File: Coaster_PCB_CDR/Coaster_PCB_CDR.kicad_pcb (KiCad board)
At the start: 2 copper layers, 96.6 x 97 mm, 31 parts, among them J1 Vin, J10 GND, J11 GND, J12 GND, J13 3v3, J14 GND, J15 GND, J2 HC-05, J3 10V, J4 Batt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

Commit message: Updated CDR PCB more
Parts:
- removed Z1: Zener, digikey-footprints:DO-214AC
- added Qat: LOGO, Coaster_PCB_CDR:pic22, F.Cu at (95.8, 129.5)
- added Qat: LOGO, Coaster_PCB_CDR:pic22, F.Cu at (159.0, 129.6)
- added Qat: LOGO, Coaster_PCB_CDR:pic22, B.Cu at (158.5, 129.5)
- added Qat: LOGO, Coaster_PCB_CDR:pic22, B.Cu at (95.2, 129.5)
- moved J2 6.80 mm to (167.7, 109.1)
- moved J9 4.28 mm to (87.0, 111.5)
- moved H2 2.26 mm to (168.0, 64.0)
- moved H1 2.00 mm to (85.2, 64.0)
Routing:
- net GPIO17: track 105.6 -> 112.8 mm
- net GPIO16: track 117.1 -> 123.3 mm, vias 0 -> 1
- net GPIO9: track 96.4 -> 100.7 mm
- net GPIO8: track 89.7 -> 94.0 mm
- net GPIO1: track 67.5 -> 71.7 mm
- net GPIO15: track 106.7 -> 108.4 mm
- net DFU: track 50.6 -> 52.3 mm
- net CTS: track 103.8 -> 104.6 mm
- net GND: vias 98 -> 108
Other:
- board size 96.6 x 97 mm -> 96.6 x 99 mm

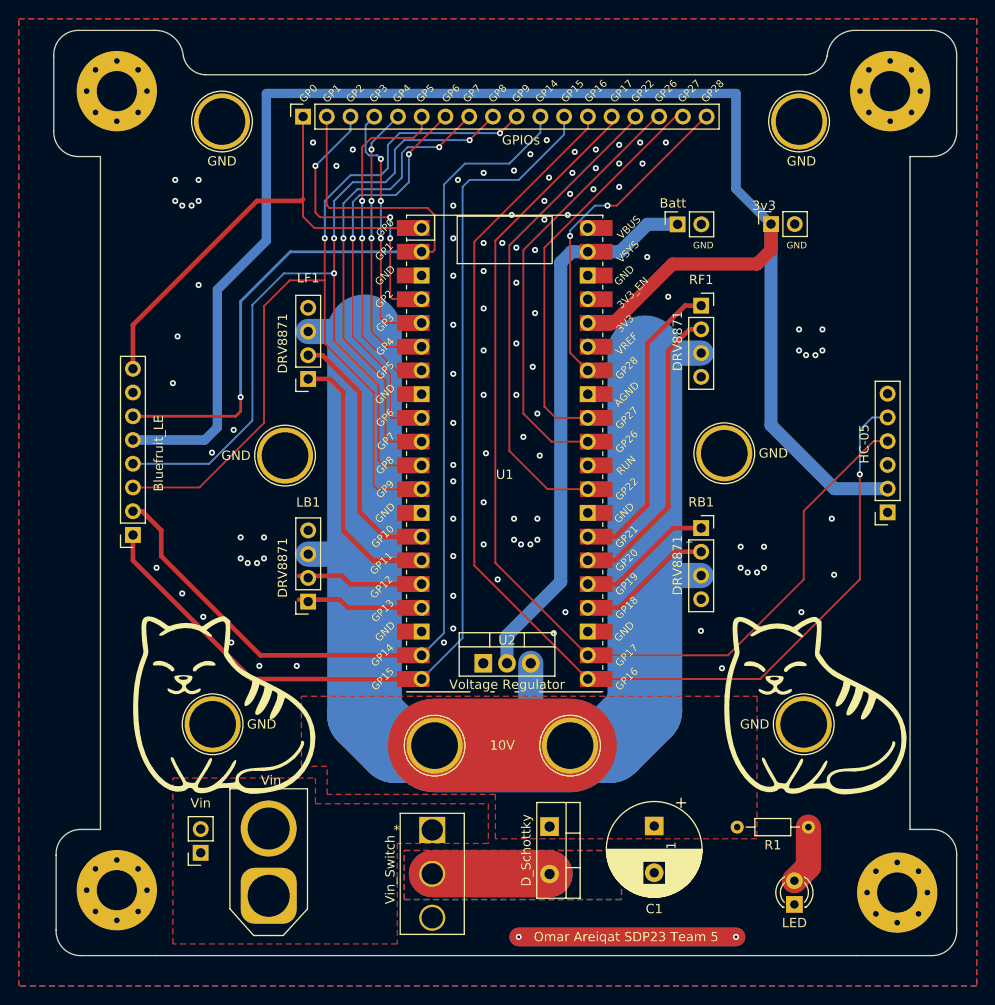
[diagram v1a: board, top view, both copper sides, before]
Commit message: Updated Polygons and Vias
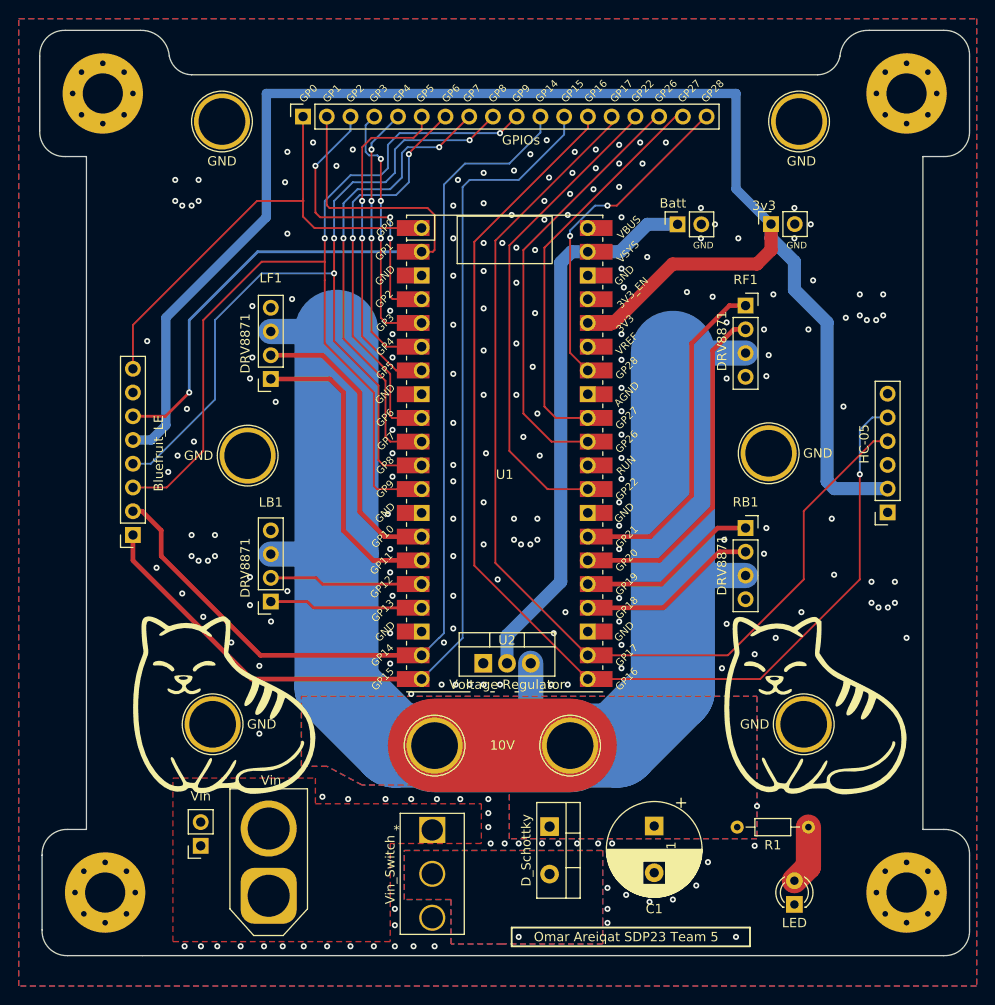
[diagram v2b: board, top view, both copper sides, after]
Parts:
- moved J10 4.75 mm to (155.0, 102.8)
- moved RB1 4.75 mm to (152.5, 110.8)
- moved RF1 4.75 mm to (152.5, 87.0)
- moved J12 4.00 mm to (99.2, 103.0)
- moved LB1 4.00 mm to (101.7, 118.6)
- moved LF1 4.00 mm to (101.7, 94.8)
- moved Qat 4.00 mm to (91.2, 129.5)
- moved H2 1.77 mm to (169.8, 64.2)
- moved H1 1.52 mm to (83.8, 64.2)
- moved H4 1.27 mm to (84.0, 149.8)
- moved H3 1.00 mm to (169.8, 149.8)
- moved J6 0.75 mm to (94.2, 144.8)
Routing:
- net (no net): track 46.5 -> 0.00 mm
- net Vcc_10v: track 25.1 -> 0.00 mm
- net +10V: track 161.6 -> 170.7 mm
- net RB1: track 14.6 -> 19.4 mm
- net RB2: track 14.6 -> 19.4 mm
- net RF2: track 32.2 -> 36.9 mm
- net RF1: track 32.5 -> 36.6 mm
- net LF2: track 27.7 -> 31.7 mm
- net LF1: track 28.8 -> 32.8 mm
- net +3V3: track 175.7 -> 172.3 mm
- net LB2: track 13.5 -> 16.4 mm
- net LB1: track 13.5 -> 16.4 mm
- net GPIO1: track 71.7 -> 69.4 mm
- net GPIO8: track 94.0 -> 91.7 mm
- net GPIO9: track 100.7 -> 102.4 mm
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- added copper zone on B.Cu, net +10V
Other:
- board size 96.6 x 99 mm -> 99.5 x 99 mm

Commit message: Updated Gerber Zip
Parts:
- moved Qat 3.25 mm to (94.5, 129.5)
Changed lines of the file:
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@@
   )
   (footprint "Coaster_PCB_CDR:pic22" (layer "B.Cu")
-    (at 91.25 129.5 180)
+    (at 94.49679 129.5 180)
     (attr board_only exclude_from_pos_files exclude_from_bom)
     (fp_text reference "Qat" (at -0.367635 -2.54) (layer "User.6")
@@
   (via (at 121.25 121.5) (size 0.65) (drill 0.3) (layers "F.Cu" "B.Cu") (free) (net 4))
   (via (at 126.5 80.25) (size 0.65) (drill 0.3) (layers "F.Cu" "B.Cu") (free) (net 4))
-  (via (at 101.75 120.75) (size 0.65) (drill 0.3) (layers "F.Cu" "B.Cu") (free) (net 4))
+  (via (at 103 121) (size 0.65) (drill 0.3) (layers "F.Cu" "B.Cu") (free) (net 4))
   (via (at 130 81) (size 0.65) (drill 0.3) (layers "F.Cu" "B.Cu") (free) (net 4))
   (via (at 139 108) (size 0.65) (drill 0.3) (layers "F.Cu" "B.Cu") (free) (net 4))

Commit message: Added some extra ground pins
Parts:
- added J16: GND, Connector_PinSocket_2.54mm:PinSocket_1x02_P2.54mm_Vertical, F.Cu at (87.0, 75.8)
- added J17: GND, Connector_PinSocket_2.54mm:PinSocket_1x02_P2.54mm_Vertical, F.Cu at (167.5, 75.5)
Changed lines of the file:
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@@
   (net 40 "CTS")
   (net 41 "DFU")
+  (footprint "Connector_PinSocket_2.54mm:PinSocket_1x02_P2.54mm_Vertical" (layer "F.Cu")
+    (at 167.5 75.46)
+    (descr "Through hole straight socket strip, 1x02, 2.54mm pitch, single row (from Kicad 4.0.7), script generated")
+    (tags "Through hole socket strip THT 1x02 2.54mm single row")
+    (property "Sheetfile" "Coaster_PCB_CDR.kicad_sch")
+    (property "Sheetname" "")
+    (attr through_hole)
+    (fp_text reference "J17" (at 0 -2.77) (layer "User.8")
+      (effects (font (size 1 1) (thickness 0.15)))
+    )
+    (fp_text value "GND" (at 0 5.31) (layer "F.SilkS")
+      (effects (font (size 1 1) (thickness 0.15)))
+    )
+    (fp_text user "${REFERENCE}" (at 0 1.27 90) (layer "F.Fab")
+      (effects (font (size 1 1) (thickness 0.15)))
+    )
+    (fp_line (start -1.33 1.27) (end 1.33 1.27) (layer "F.SilkS") (width 0.12))
+    (fp_line (start -1.33 1.27) (end -1.33 3.87) (layer "F.SilkS") (width 0.12))
+    (fp_line (start -1.33 3.87) (end 1.33 3.87) (layer "F.SilkS") (width 0.12))
+    (fp_line (start 1.33 -1.33) (end 1.33 0) (layer "F.SilkS") (width 0.12))
+    (fp_line (start 0 -1.33) (end 1.33 -1.33) (layer "F.SilkS") (width 0.12))
+    (fp_line (start 1.33 1.27) (end 1.33 3.87) (layer "F.SilkS") (width 0.12))
+    (fp_line (start -1.8 4.3) (end -1.8 -1.8) (layer "F.CrtYd") (width 0.05))
+    (fp_line (start -1.8 -1.8) (end 1.75 -1.8) (layer "F.CrtYd") (width 0.05))
+    (fp_line (start 1.75 4.3) (end -1.8 4.3) (layer "F.CrtYd") (width 0.05))
+    (fp_line (start 1.75 -1.8) (end 1.75 4.3) (layer "F.CrtYd") (width 0.05))
+    (fp_line (start -1.27 3.81) (end -1.27 -1.27) (layer "F.Fab") (width 0.1))
+    (fp_line (start 1.27 3.81) (end -1.27 3.81) (layer "F.Fab") (width 0.1))
+    (fp_line (start 0.635 -1.27) (end 1.27 -0.635) (layer "F.Fab") (width 0.1))
+    (fp_line (start -1.27 -1.27) (end 0.635 -1.27) (layer "F.Fab") (width 0.1))
+    (fp_line (start 1.27 -0.635) (end 1.27 3.81) (layer "F.Fab") (width 0.1))
+    (pad "1" thru_hole rect (at 0 0) (size 1.7 1.7) (drill 1) (layers *.Cu *.Mask)
+      (net 4 "GND") (pinfunction "Pin_1") (pintype "passive"))
+    (pad "2" thru_hole oval (at 0 2.54) (size 1.7 1.7) (drill 1) (layers *.Cu *.Mask)
+      (net 4 "GND") (pinfunction "Pin_2") (pintype "passive"))
+    (model "${KICAD6_3DMODEL_DIR}/Connector_PinSocket_2.54mm.3dshapes/PinSocket_1x02_P2.54mm_Vertical.wrl"
+      (offset (xyz 0 0 0))
+      (scale (xyz 1 1 1))
+      (rotate (xyz 0 0 0))
+    )
+  )
   (footprint "TestPoint:TestPoint_Plated_Hole_D5.0mm" (layer "F.Cu")
     (at 95.5 131.75)
@@
       (net 4 "GND") (pinfunction "1") (pintype "input"))
   )
+  (footprint "Connector_PinSocket_2.54mm:PinSocket_1x02_P2.54mm_Vertical" (layer "F.Cu")
+    (at 87.025 75.75)
+    (descr "Through hole straight socket strip, 1x02, 2.54mm pitch, single row (from Kicad 4.0.7), script generated")
+    (tags "Through hole socket strip THT 1x02 2.54mm single row")
+    (property "Sheetfile" "Coaster_PCB_CDR.kicad_sch")
+    (property "Sheetname" "")
+    (attr through_hole)
+    (fp_text reference "J16" (at 0 -2.77) (layer "User.4")
+      (effects (font (size 1 1) (thickness 0.15)))
+    )
+    (fp_text value "GND" (at 0 5.31) (layer "F.Fab")
+      (effects (font (size 1 1) (thickness 0.15)))
+    )
+    (fp_text user "${REFERENCE}" (at 0 1.27 90) (layer "F.Fab")
+      (effects (font (size 1 1) (thickness 0.15)))
+    )
+    (fp_line (start 1.33 1.27) (end 1.33 3.87) (layer "F.SilkS") (width 0.12))
+    (fp_line (start -1.33 1.27) (end -1.33 3.87) (layer "F.SilkS") (width 0.12))
+    (fp_line (start 0 -1.33) (end 1.33 -1.33) (layer "F.SilkS") (width 0.12))
+    (fp_line (start -1.33 3.87) (end 1.33 3.87) (layer "F.SilkS") (width 0.12))
+    (fp_line (start 1.33 -1.33) (end 1.33 0) (layer "F.SilkS") (width 0.12))
+    (fp_line (start -1.33 1.27) (end 1.33 1.27) (layer "F.SilkS") (width 0.12))
+    (fp_line (start 1.75 -1.8) (end 1.75 4.3) (layer "F.CrtYd") (width 0.05))
+    (fp_line (start -1.8 4.3) (end -1.8 -1.8) (layer "F.CrtYd") (width 0.05))
+    (fp_line (start -1.8 -1.8) (end 1.75 -1.8) (layer "F.CrtYd") (width 0.05))
+    (fp_line (start 1.75 4.3) (end -1.8 4.3) (layer "F.CrtYd") (width 0.05))
+    (fp_line (start 0.635 -1.27) (end 1.27 -0.635) (layer "F.Fab") (width 0.1))
+    (fp_line (start -1.27 -1.27) (end 0.635 -1.27) (layer "F.Fab") (width 0.1))
+    (fp_line (start 1.27 -0.635) (end 1.27 3.81) (layer "F.Fab") (width 0.1))
+    (fp_line (start 1.27 3.81) (end -1.27 3.81) (layer "F.Fab") (width 0.1))
+    (fp_line (start -1.27 3.81) (end -1.27 -1.27) (layer "F.Fab") (width 0.1))
+    (pad "1" thru_hole rect (at 0 0) (size 1.7 1.7) (drill 1) (layers *.Cu *.Mask)
+      (net 4 "GND") (pinfunction "Pin_1") (pintype "passive"))
+    (pad "2" thru_hole oval (at 0 2.54) (size 1.7 1.7) (drill 1) (layers *.Cu *.Mask)
+      (net 4 "GND") (pinfunction "Pin_2") (pintype "passive"))
+    (model "${KICAD6_3DMODEL_DIR}/Connector_PinSocket_2.54mm.3dshapes/PinSocket_1x02_P2.54mm_Vertical.wrl"
+      (offset (xyz 0 0 0))
+      (scale (xyz 1 1 1))
+      (rotate (xyz 0 0 0))
+    )
+  )
   (footprint "Connector_AMASS:AMASS_XT60-M_1x02_P7.20mm_Vertical" (layer "F.Cu")
     (at 101.5 150.1 90)
@@
     (effects (font (size 0.8 0.8) (thickness 0.15)))
   )
+  (gr_text "GND" (at 87.025 73.25) (layer "F.SilkS")
+    (effects (font (size 1 1) (thickness 0.15)))
+  )
   (gr_text "GND" (at 148 80.5) (layer "F.SilkS")
     (effects (font (size 0.7 0.7) (thickness 0.175)))
@@
     (effects (font (size 1 1) (thickness 0.25)))
   )
+  (gr_text "GND" (at 167.5 72.75) (layer "F.SilkS")
+    (effects (font (size 1 1) (thickness 0.15)))
+  )
   (gr_text "GP14" (at 131.25 64 45) (layer "F.SilkS")
     (effects (font (size 0.8 0.8) (thickness 0.15)))
@@
     (effects (font (size 0.8 0.8) (thickness 0.15)))
   )
+  (gr_text "GND" (at 87 81) (layer "F.SilkS")
+    (effects (font (size 1 1) (thickness 0.15)))
+  )
   (gr_text "GP1" (at 108.25 64.25 45) (layer "F.SilkS")

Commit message: Minor Updates, requested order
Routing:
- net GPIO16: track 123.3 -> 125.3 mm, vias 1 -> 3
- net GPIO17: track 112.8 -> 114.0 mm
- net GPIO7: track 49.8 -> 50.6 mm, vias 2 -> 3
- net GPIO9: track 102.4 -> 103.1 mm, vias 2 -> 3
- net GPIO8: track 91.7 -> 92.5 mm, vias 3 -> 4
- net GPIO6: track 43.5 -> 44.3 mm, vias 2 -> 3
- net GPIO5: track 36.7 -> 37.4 mm, vias 2 -> 3
- net GPIO4: track 30.2 -> 31.0 mm, vias 3 -> 4
- net GPIO3: track 27.7 -> 28.4 mm, vias 3 -> 4
- net GPIO2: track 30.4 -> 31.2 mm, vias 3 -> 4

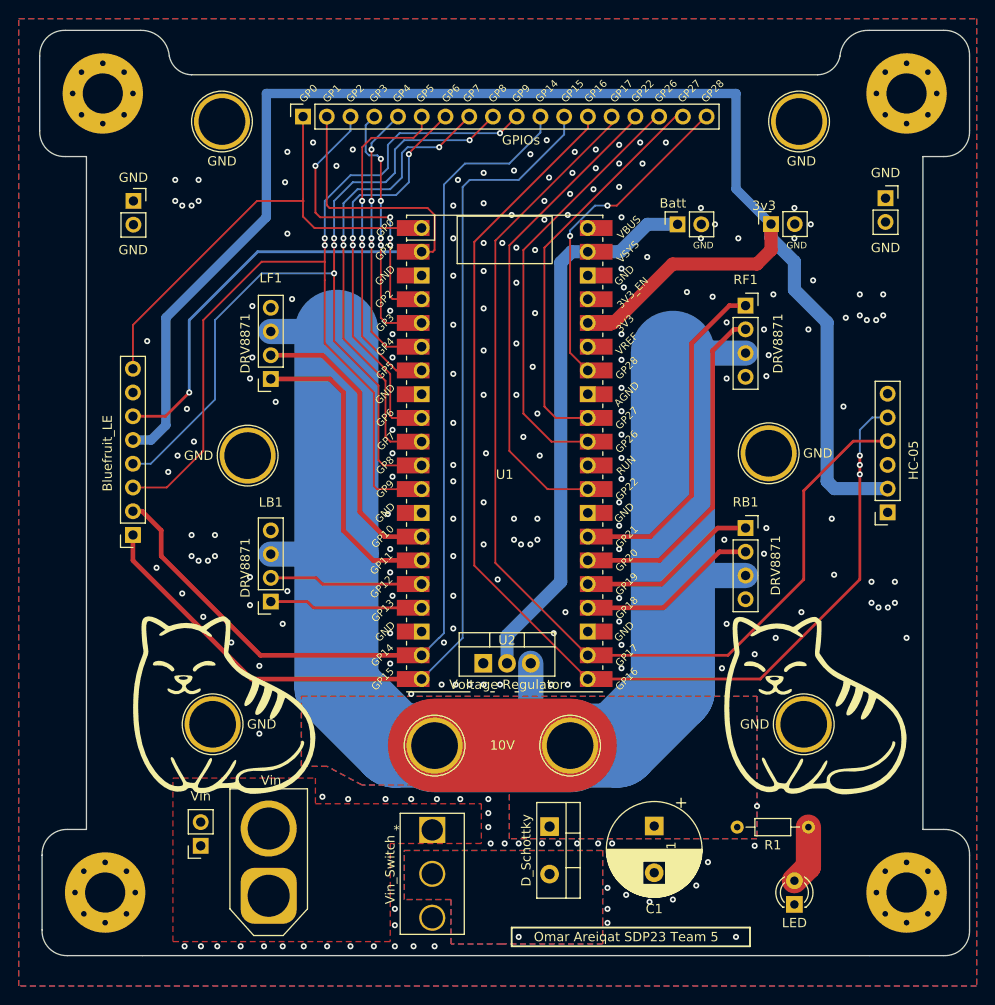
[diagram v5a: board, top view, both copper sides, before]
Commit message: fixed overlapping zones
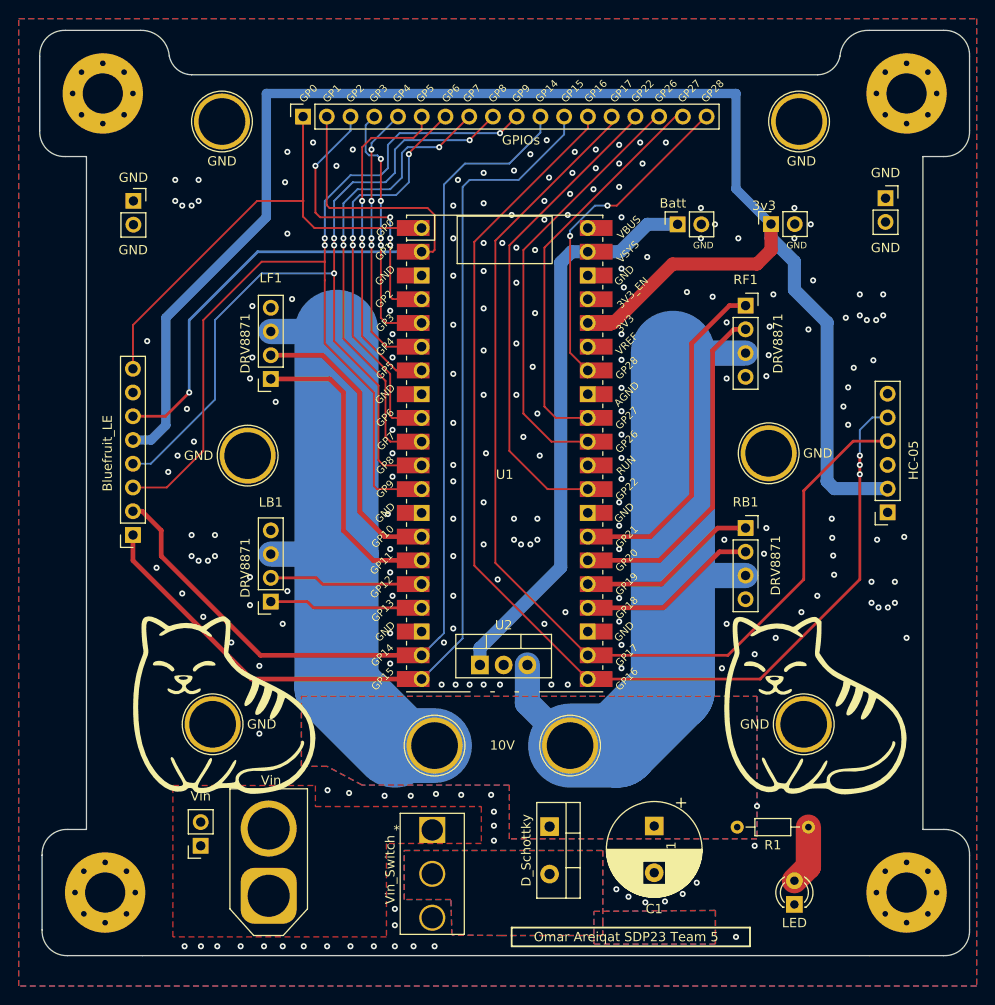
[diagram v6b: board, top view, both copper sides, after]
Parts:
- U2: value Voltage Regulator -> LM2937xT
- moved U2 0.40 mm to (124.1, 125.4)
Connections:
- U2 pad 1: GND -> VSYS
- U2 pad 2: VSYS -> GND
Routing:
- net +10V: track 170.7 -> 141.7 mm
- net VSYS: track 59.5 -> 60.8 mm
- net GND: vias 224 -> 223
- net (no net): vias 2 -> 1

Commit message: removed pico smd pads
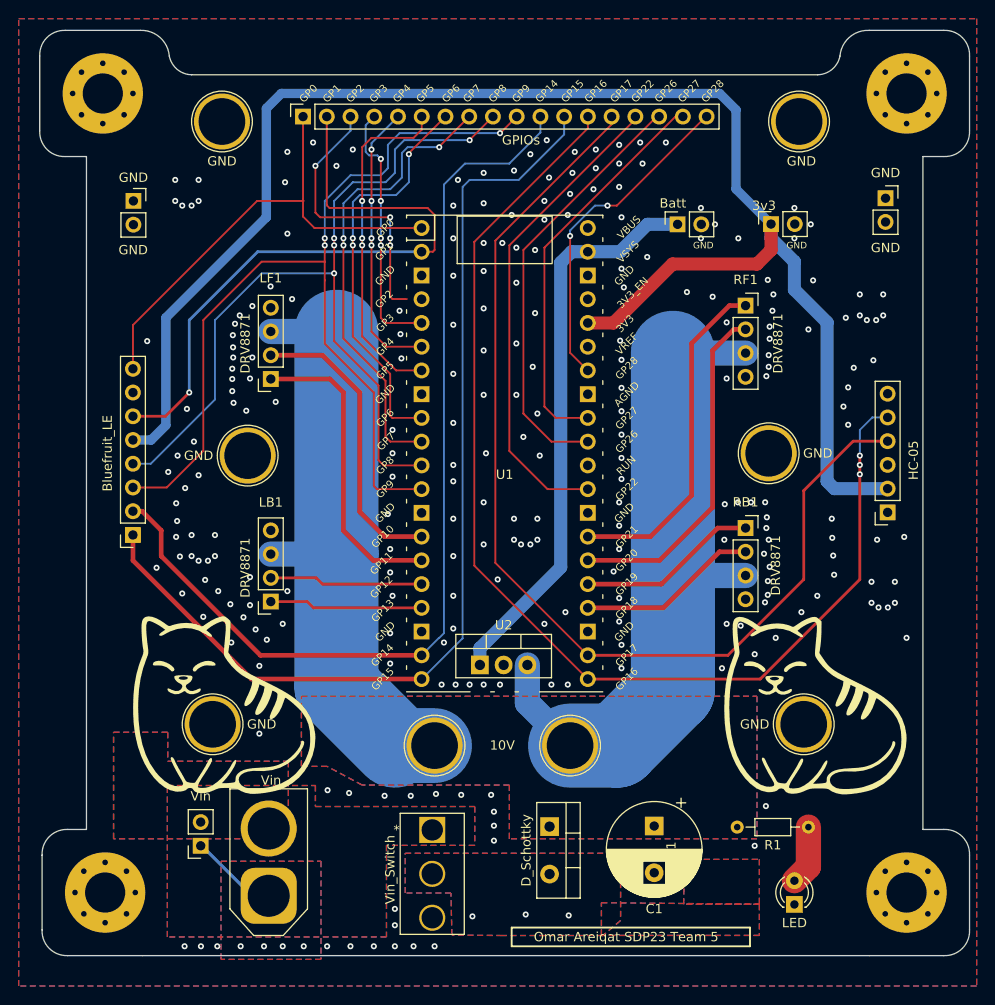
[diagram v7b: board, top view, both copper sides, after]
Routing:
- net GND: track 0.00 -> 9.49 mm, vias 223 -> 256
- net +3V3: track 172.3 -> 170.4 mm
- net Vcc_10v: vias 0 -> 3
- net (no net): vias 1 -> 0
- added copper zone on B.Cu, net VCC

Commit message: added more polygons
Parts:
- removed J11, J14: GND, TestPoint:TestPoint_Plated_Hole_D5.0mm
- moved D3 16.8 mm to (161.9, 134.8), turned to 0 degrees
- moved R1 14.7 mm to (166.9, 130.2)
- moved D1 0.34 mm to (131.6, 142.4)
- moved C1 0.33 mm to (142.8, 142.3), turned to 0 degrees
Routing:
- net +10V: track 141.7 -> 0.00 mm
- net GPIO2: track 31.2 -> 32.8 mm
- net Net-(D3-Pad2): track 6.36 -> 5.61 mm
- net RF2: track 36.9 -> 36.4 mm
- net Vcc_10v: vias 3 -> 0
- net GND: vias 256 -> 273
